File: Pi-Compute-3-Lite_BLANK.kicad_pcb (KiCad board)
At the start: 2 copper layers, 33 parts, among them J1 USB_OTG, J2 USB_OTG, U1 PAM2306AYPKE, U2 AP7115-25SEG, U3 DDR2_SODIMM_CM_3_Lite, U4 1040310811

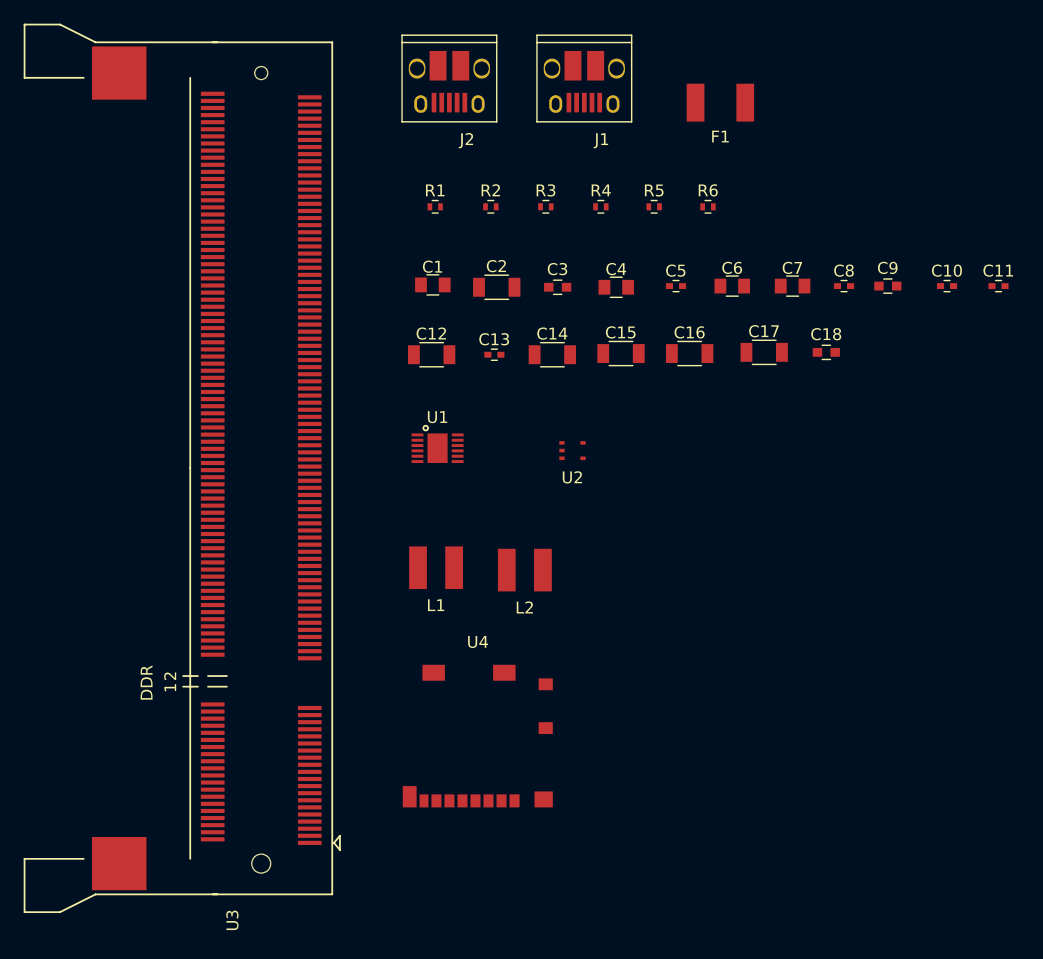
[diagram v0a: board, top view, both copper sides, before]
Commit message: Added suggested power supply layout to PCB
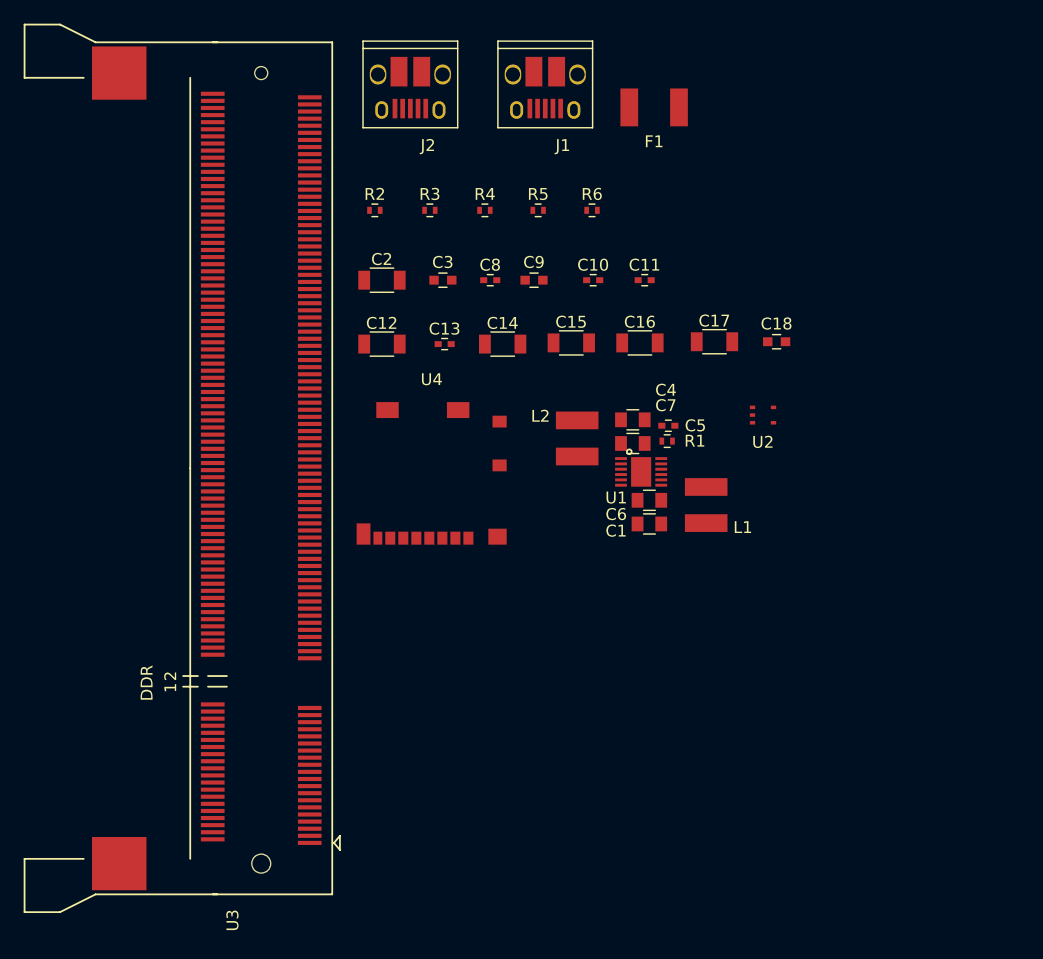
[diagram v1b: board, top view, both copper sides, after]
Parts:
- moved C10 29.9 mm to (113.8, 72.6)
- moved C11 29.9 mm to (118.1, 72.6)
- moved C9 29.9 mm to (108.8, 72.6)
- moved C8 29.9 mm to (105.0, 72.6)
- moved R1 27.9 mm to (120.0, 86.2), turned to 180 degrees
- moved C1 27.3 mm to (118.5, 93.2), turned to 180 degrees
- moved L1 23.4 mm to (123.3, 91.6), turned to 270 degrees
- moved U4 22.5 mm to (100.1, 94.4)
- moved C6 19.4 mm to (118.5, 91.2), turned to 180 degrees
- moved C7 19.0 mm to (117.1, 86.4)
- moved U1 17.3 mm to (117.8, 88.8)
- moved U2 16.4 mm to (128.1, 84.0)
- moved L2 12.0 mm to (112.4, 86.0), turned to 90 degrees
- moved C5 11.8 mm to (120.1, 84.9)
- moved C4 11.3 mm to (117.1, 84.4)
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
